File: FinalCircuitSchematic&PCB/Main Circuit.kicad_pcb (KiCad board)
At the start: 6 copper layers, 65.2 x 30.1 mm, 86 parts, among them IC1 LTC3895IFE#TRPBF, J1 Conn_01x02_Male, J2 Conn_01x02_Male, J3 Conn_01x02_Male, J4 Raspberry_Pi_2_3, J5 Conn_01x02_Male, J6 Conn_01x02_Male, J7 Conn_01x02_Male, J8 Conn_01x02_Male, Q1 PN2222A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

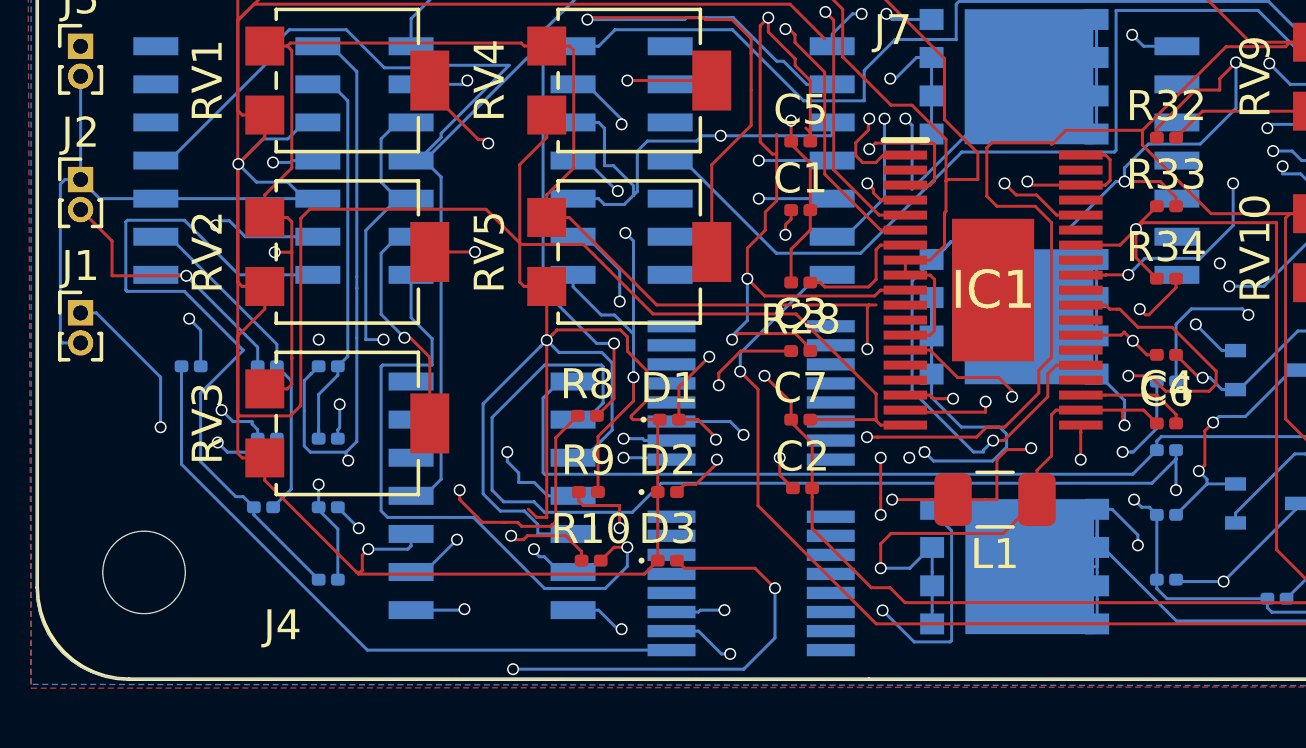
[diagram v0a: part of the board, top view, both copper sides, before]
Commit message: Updated final schematic as incorrect switch packages were selected. Added external switch library
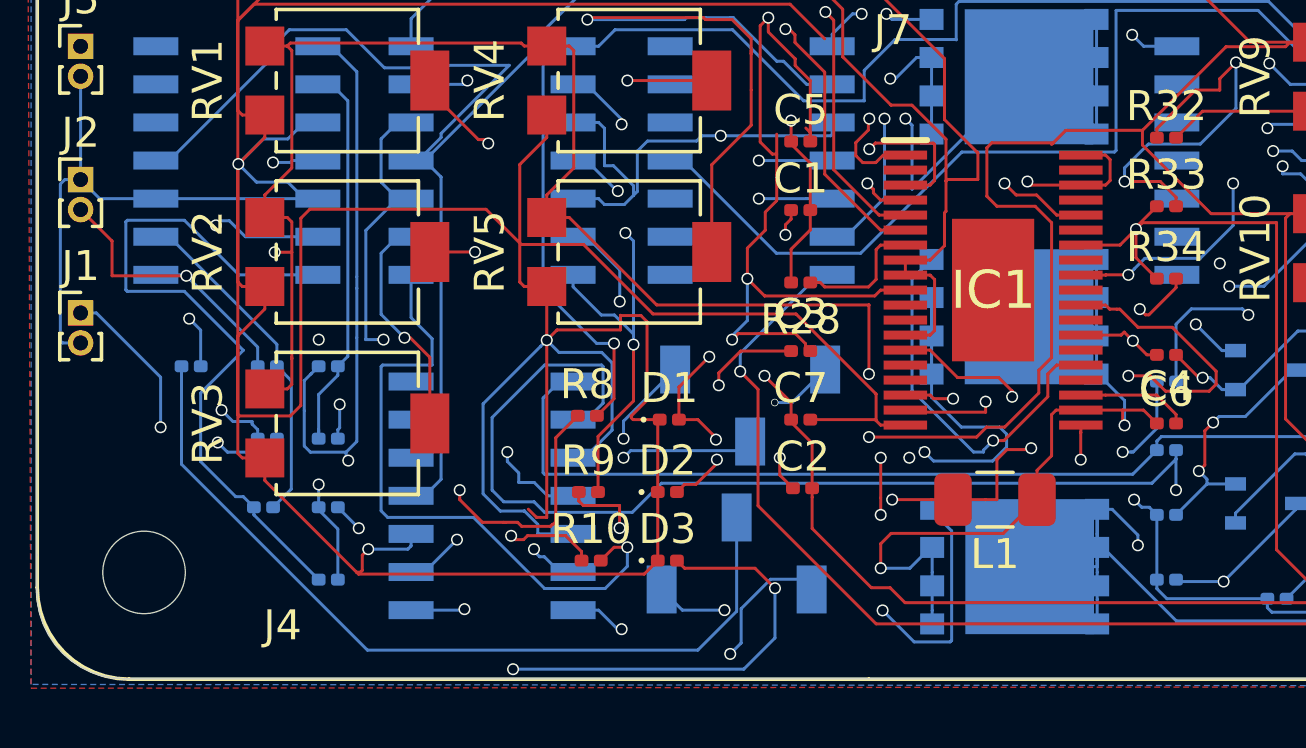
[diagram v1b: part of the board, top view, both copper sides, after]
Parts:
- removed U8, U9: Switch, Package_SO:QSOP-16_3.9x4.9mm_P0.635mm
- added SW1: SW_SPDT, Button_Switch_SMD:JS102011JCQN, B.Cu at (65.7, 53.4)
- added SW2: SW_SPDT, Button_Switch_SMD:JS102011JCQN, B.Cu at (66.1, 47.9)
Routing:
- net Net-(R11-Pad1): track 22.2 -> 28.0 mm
- net Net-(R29-Pad1): track 34.3 -> 37.1 mm
- net Net-(IC1-Pad6): track 52.6 -> 50.2 mm
- net Net-(SW1-Pad1): track 31.6 -> 33.9 mm
- net Net-(IC1-Pad24): track 14.6 -> 12.8 mm
- net Net-(SW2-Pad1): track 64.6 -> 65.9 mm
- net GND: track 466.8 -> 468.2 mm
- net Net-(IC1-Pad28): track 63.2 -> 64.5 mm
- net Net-(SW2-Pad3): track 43.9 -> 42.6 mm
- net Net-(J6-Pad2): track 90.0 -> 90.6 mm
- net Net-(SW1-Pad3): track 30.3 -> 30.9 mm
